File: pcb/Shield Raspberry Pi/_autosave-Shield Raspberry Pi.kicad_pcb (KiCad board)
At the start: 2 copper layers, 65 x 56 mm, 58 parts, among them J1 , J10 , J2 , J3 , J4 , J5 , J6 , J7 , J8 , J9 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

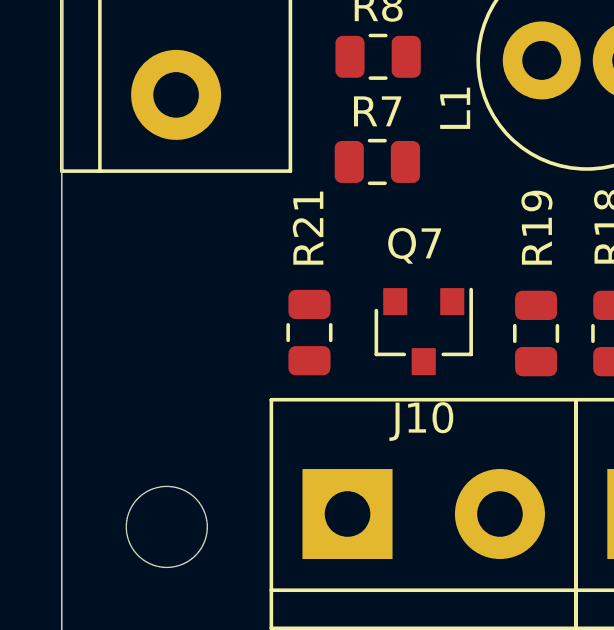
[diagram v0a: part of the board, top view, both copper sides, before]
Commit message: Falta el ruteo, todo el resto está listo
Se completó el modelado 3D, se ubicaron todos los componentes, solo falta el ruteo
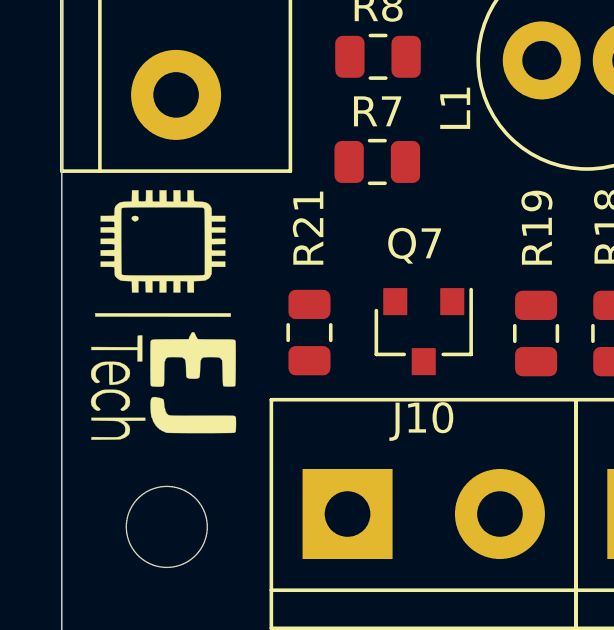
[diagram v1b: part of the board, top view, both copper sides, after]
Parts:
- added  : , Symbol:EJ TECH 8X5.5, F.Cu at (126.4, 117.5)
- added  : , Symbol:EJ TECH 18X11, B.Cu at (146.4, 101.2)
